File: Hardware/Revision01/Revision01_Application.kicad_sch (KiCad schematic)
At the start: 59 parts, among them J2 StrainConn, J3 StrainConn, J4 StrainConn, J5 StrainConn, J6 StrainConn, J7 StrainConn, J8 StrainConn, J9 StrainConn, Q3 NMOS, Q4 PMOS, Q6 PMOS, U11 LP5813BDRRR, U2 MRF89XAM9AT-I/RM, U4 ICM-45605, U6 INA317xxDGK

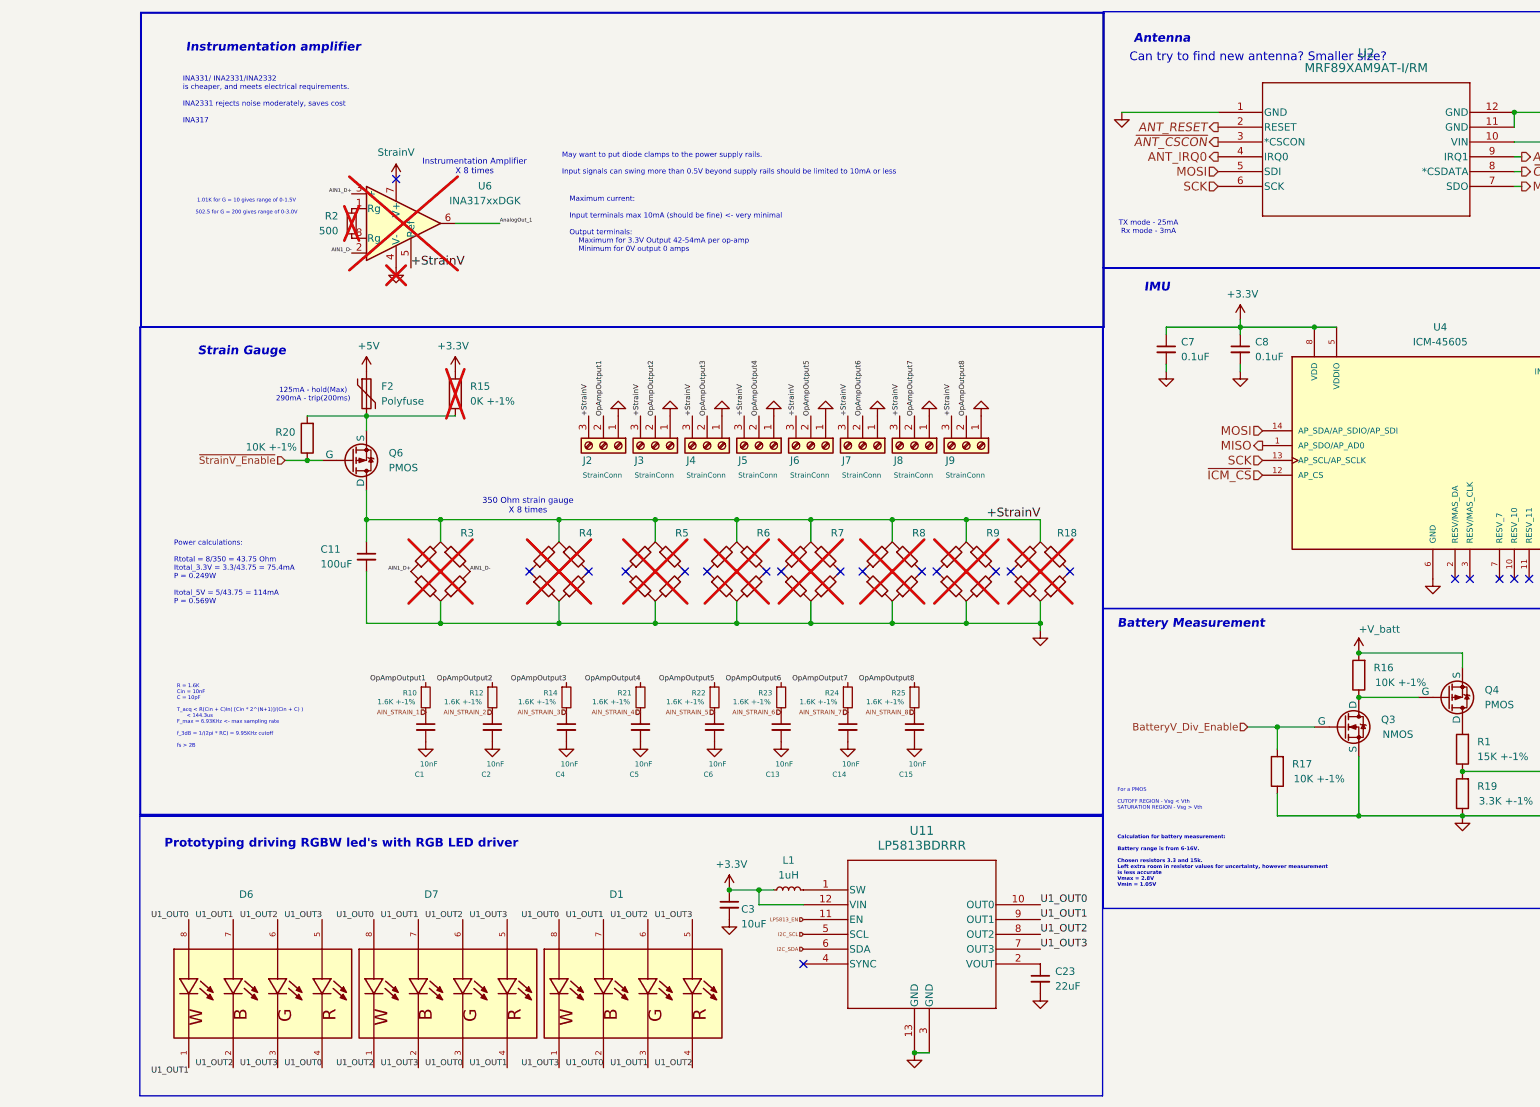
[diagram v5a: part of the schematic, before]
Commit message: schematic wiring, and LT-SPICE simulations on strain gauge - Added buffer with offset at 1.66V to instrumentation amplifier to ensure -20-20mv range can be read - Added caps to Instrumentation Amplifier circuit - Stimulated straingauge->Amplifier->Adc with all components imported. Verified ADC can read between 0.3-3.0V - Created second draft bom, component cost at around 212$ - Changed many components to Automotive grade - Added breathingCUBE led driver to prototype my own project
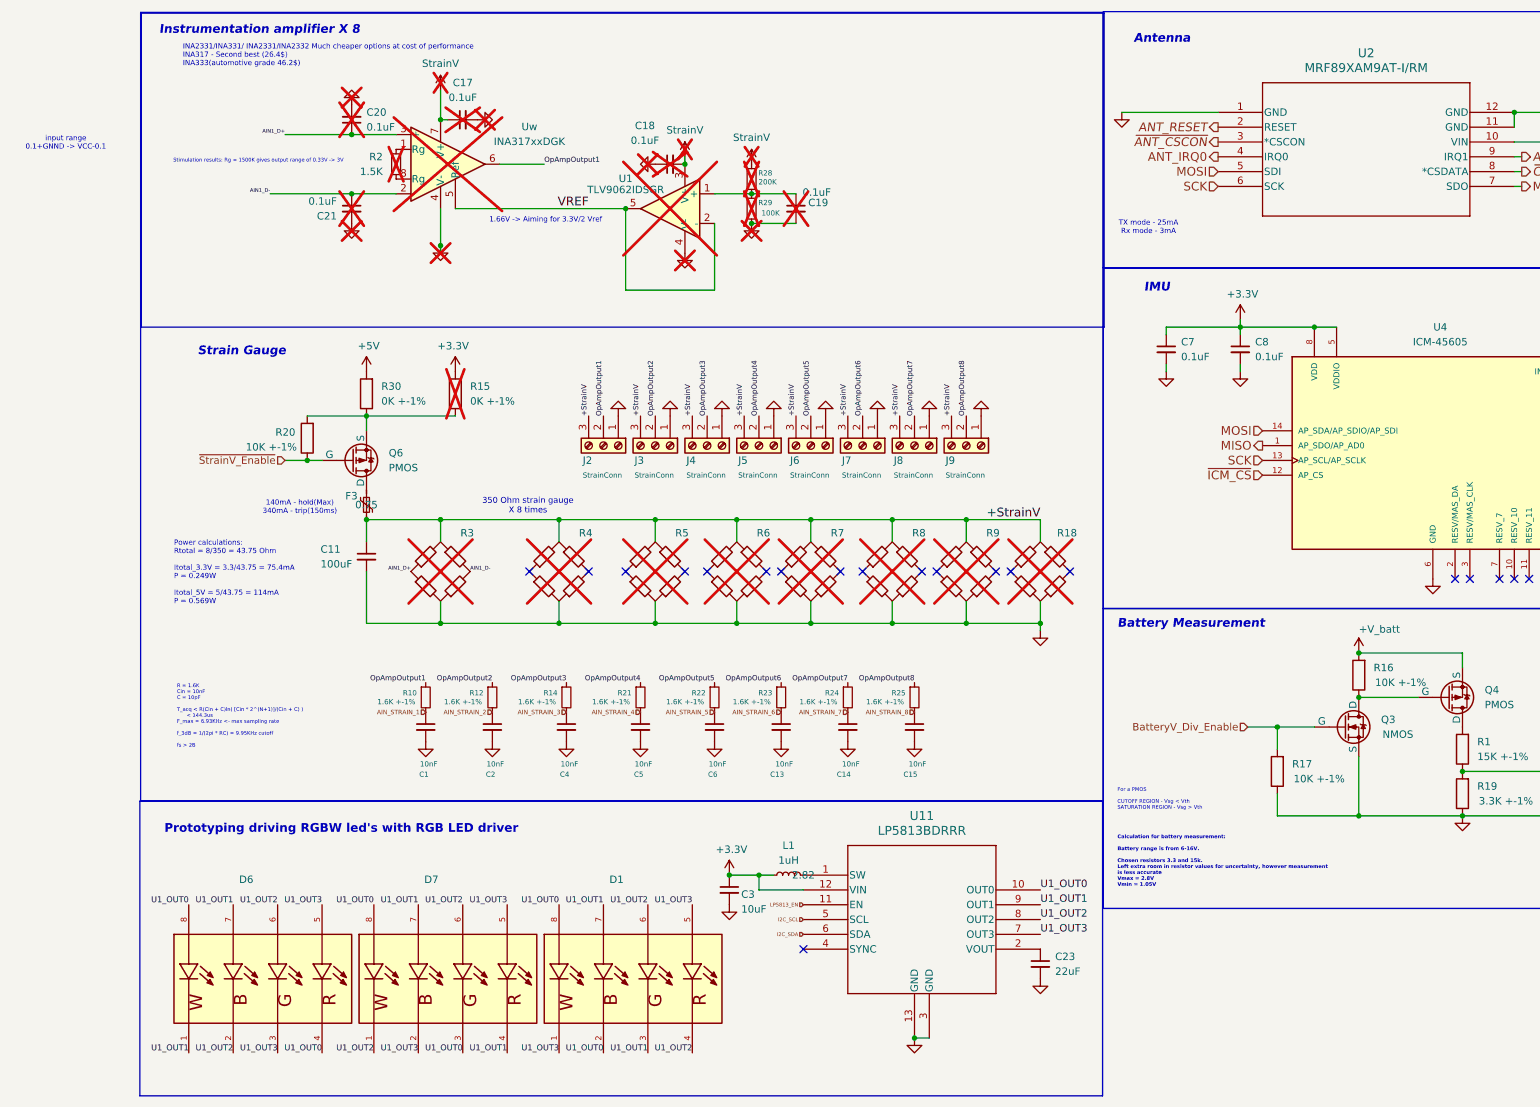
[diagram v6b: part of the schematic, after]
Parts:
- removed F2: Polyfuse, Resistor_SMD:R_1206_3216Metric_Pad1.30x1.75mm_HandSolder, symbol Device:Polyfuse
- added C17, C18, C19, C20, C21: 0.1uF, Capacitor_SMD:C_0805_2012Metric_Pad1.18x1.45mm_HandSolder, symbol Device:C_Small
- added F3: Polyfuse_Small, Resistor_SMD:R_1812_4532Metric_Pad1.30x3.40mm_HandSolder, symbol Device:Polyfuse_Small
- added R28: 200K, Resistor_SMD:R_0603_1608Metric_Pad0.98x0.95mm_HandSolder, symbol Device:R_Small
- added R29: 100K, Resistor_SMD:R_0603_1608Metric_Pad0.98x0.95mm_HandSolder, symbol Device:R_Small
- added R30: 0K +-1%, Resistor_SMD:R_1206_3216Metric_Pad1.30x1.75mm_HandSolder, symbol Device:R
- added U1: TLV9062IDSGR, symbol Simulation_SPICE:OPAMP
- C1, C13, C14, C15, C2, C4, C5, C6: Price per unit (none) -> 0.24700
- C10: Price per unit 0.15 -> 4; Quantity 3 -> (none)
- C11, Q3, R19, U2, U4: Quantity 1 -> (none)
- C12, C7, C8, C9: Distributor link https://www.digikey.ca/en/products/detail/yageo/CC0805JRNPO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 -> https://www.digikey.ca/en/products/detail/murata-electronic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; Manufacturer Samsung Electro-Mechanics -> Murata Electronics; Manufacturer Part Number CL05B104KA5NNNC -> GCM155R71C104KA55J; Price per unit 0.12 -> 0.043; Quantity 23 -> (none)
- C23: Price per unit (none) -> 0.12000
- C3: Distributor link (none) -> https://www.digikey.ca/en/products/detail/murata-electronic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; Manufacturer Part Number (none) -> CL31B106KAHNNNE; Price per unit (none) -> 4
- D1, D6, D7: Distributor link (none) -> https://www.digikey.ca/en/products/detail/qt-brightek-qtb/Q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; Price per unit (none) -> 1.19000
- L1: Price per unit (none) -> 0.36000
- Q4, Q6: Quantity 2 -> (none)
- R1: footprint Resistor_SMD:R_0805_2012Metric -> Resistor_SMD:R_0603_1608Metric_Pad0.98x0.95mm_HandSolder; Quantity 1 -> (none)
- R10, R12, R14, R21, R22, R23, R24, R25: footprint Resistor_SMD:R_0815_2038Metric -> Resistor_SMD:R_0402_1005Metric_Pad0.72x0.64mm_HandSolder; Distributor link https://www.digikey.ca/en/products/detail/yageo/RC0805FR-07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 -> https://www.digikey.ca/en/products/detail/yageo/RC0402FR-07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; Manufacturer Part Number RC0805FR-071K6L -> RC0402FR-071K6L; Price per unit (none) -> 0.012
- R15: Price per unit 0.42 -> 0.27; Quantity 2 -> (none)
- R16, R17: footprint Resistor_SMD:R_2512_6332Metric_Pad1.40x3.35mm_HandSolder -> Resistor_SMD:R_0603_1608Metric_Pad0.98x0.95mm_HandSolder; Distributor link https://www.digikey.ca/en/products/detail/yageo/RC0805FR-07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 -> https://www.digikey.ca/en/products/detail/bourns-inc/CR0603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; Manufacturer (none) -> Bourns Inc; Manufacturer Part Number CRGCQ2512F10K -> CR0603-FX-1002ELF; Quantity 3 -> (none)
- R2: value 500 -> 1.5K; Distributor link (none) -> https://www.mouser.ca/ProductDetail/KOA-Speer/RN73H1JTTD150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; Manufacturer (none) -> KOA Speer; Manufacturer Part Number (none) -> RT0603BRC07500RL; Price per unit (none) -> 0.098
- R20: footprint Resistor_SMD:R_2512_6332Metric_Pad1.40x3.35mm_HandSolder -> Resistor_SMD:R_0603_1608Metric_Pad0.98x0.95mm_HandSolder; Distributor link https://www.digikey.ca/en/products/detail/te-connectivity-p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 -> https://www.digikey.ca/en/products/detail/bourns-inc/CR0603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; Manufacturer (none) -> Bourns Inc; Manufacturer Part Number CRGCQ2512F10K -> CR0603-FX-1002ELF; Quantity 3 -> (none)
- U11: Distributor link (none) -> https://www.mouser.ca/ProductDetail/Texas-Instruments/LP581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; Price per unit (none) -> 2.82
- Uw: renamed from U6; Distributor link (none) -> https://www.mouser.ca/ProductDetail/Texas-Instruments/INA31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; Manufacturer (none) -> Texas Instruments; Manufacturer Part Number (none) -> INA317IDGKR; Price per unit (none) -> 2.64
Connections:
- net AnalogOut_1 is gone; now on net OpAmpOutput1: Uw.6
- net +5V: now also R30.2
- net +StrainV: now also F3.2; no longer Q6.1 (D), Uw.5 (Ref)
- net AIN1_D+: now also C20.1
- net AIN1_D-: now also C21.1
- net GND: now also C17.2, C18.1, C19.2, C20.2, C21.2, R29.2, U1.4 (V-)
- net U1_OUT1: now also D6.1
- net at Q6.3 (S), R15.1, R20.2: now also R30.1
- net at Uw.7 (V+): now also C17.1
- new net: F3.1, Q6.1 (D)
- new net: C19.1, R28.2, R29.1, U1.1 (+)
- new net: C18.2, U1.3 (V+)
- new net VREF: U1.2 (-), U1.5, Uw.5 (Ref)
- no-connect marks 21 -> 20
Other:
- note added: "1.66V -> Aiming for 3.3V/2 Vref"
- note added: "140mA - hold(Max) 340mA - trip(150ms)"
- note added: "INA2331/INA331/ INA2331/INA2332 Much cheaper options at cost of performance INA317 - Second best (26.4$) INA333(automotive grade 46.2$)"
- note added: "Instrumentation amplifier X 8"
- note added: "Stimulation results: Rg = 1500K gives output range of 0.33V -> 3V"
- note added: "input range 0.1+GNND -> VCC-0.1"
- note removed: "1.01K for G = 10 gives range of 0-1.5V 502.5 for G = 200 gives range of 0-3.0V"
- note removed: "125mA - hold(Max) 290mA - trip(200ms)"
- note removed: "Can try to find new antenna? Smaller size?"
- note removed: "INA331/ INA2331/INA2332 is cheaper, and meets electrical requirements. INA2331 rejects noise moderately, saves cost INA317"
- note removed: "Instrumentation Amplifier X 8 times"
- note removed: "Instrumentation amplifier"
- note removed: "Maximum current: Input terminals max 10mA (should be fine) <- very minimal Output terminals: Maximum for 3.3V Output 42-54mA per op-amp Minimum for 0V output 0 amps"
- note removed: "May want to put diode clamps to the power supply rails. Input signals can swing more than 0.5V beyond supply rails should be limited to 10mA or less"
- moved on the sheet: C23, C3, D1, D6, D7, L1, R2, U11, Uw

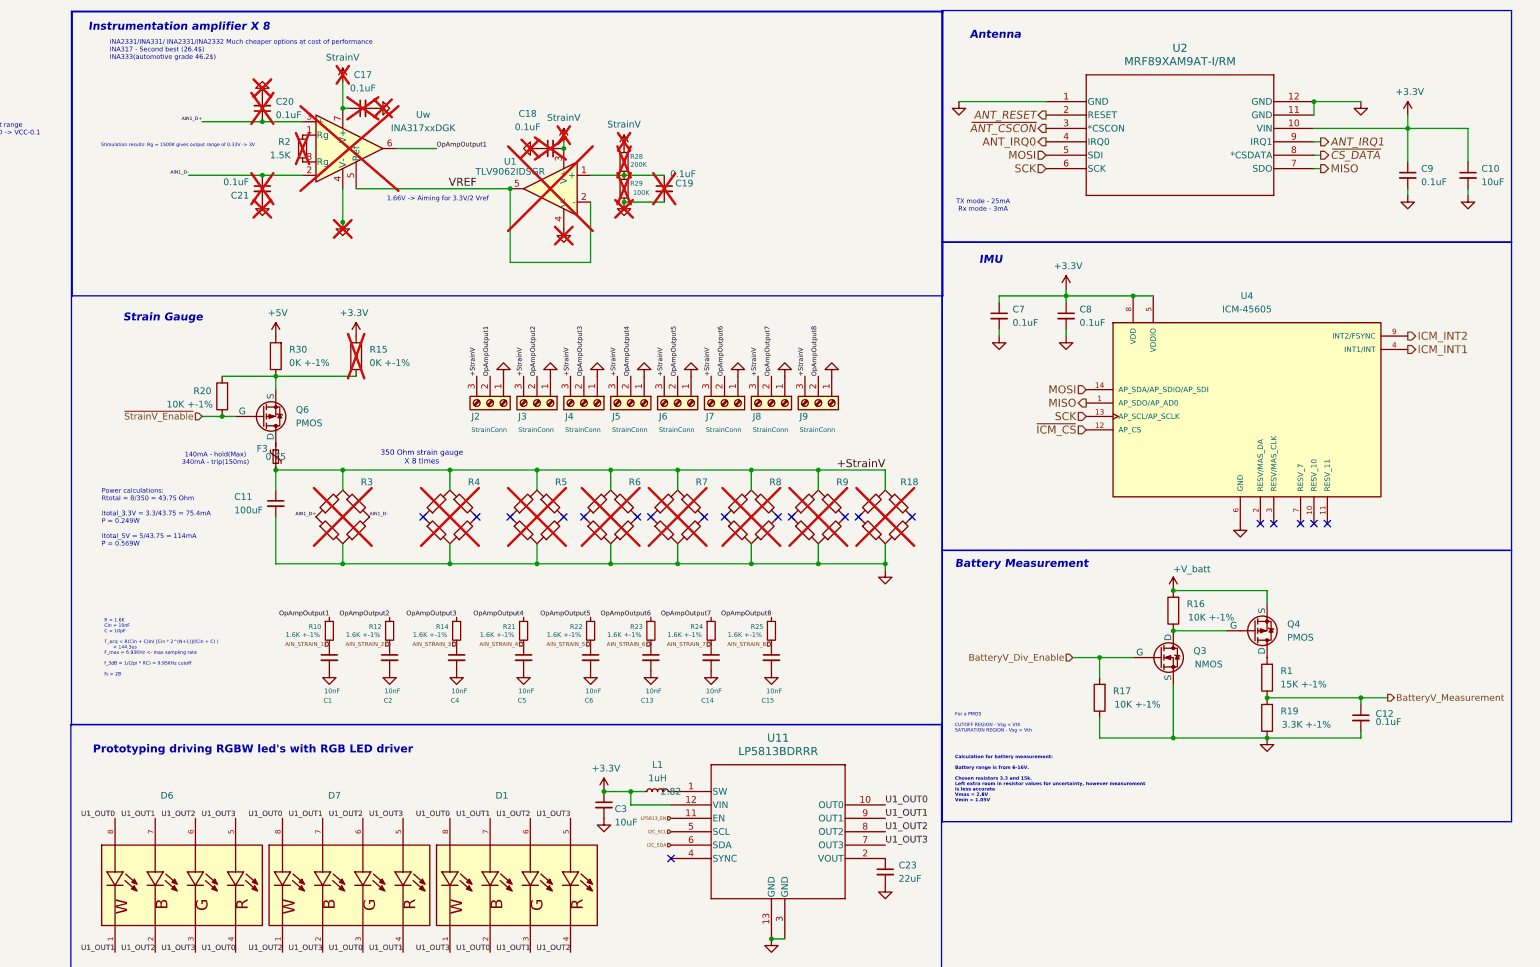
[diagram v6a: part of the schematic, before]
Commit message: branch fuses selected. Ready for PCB layout
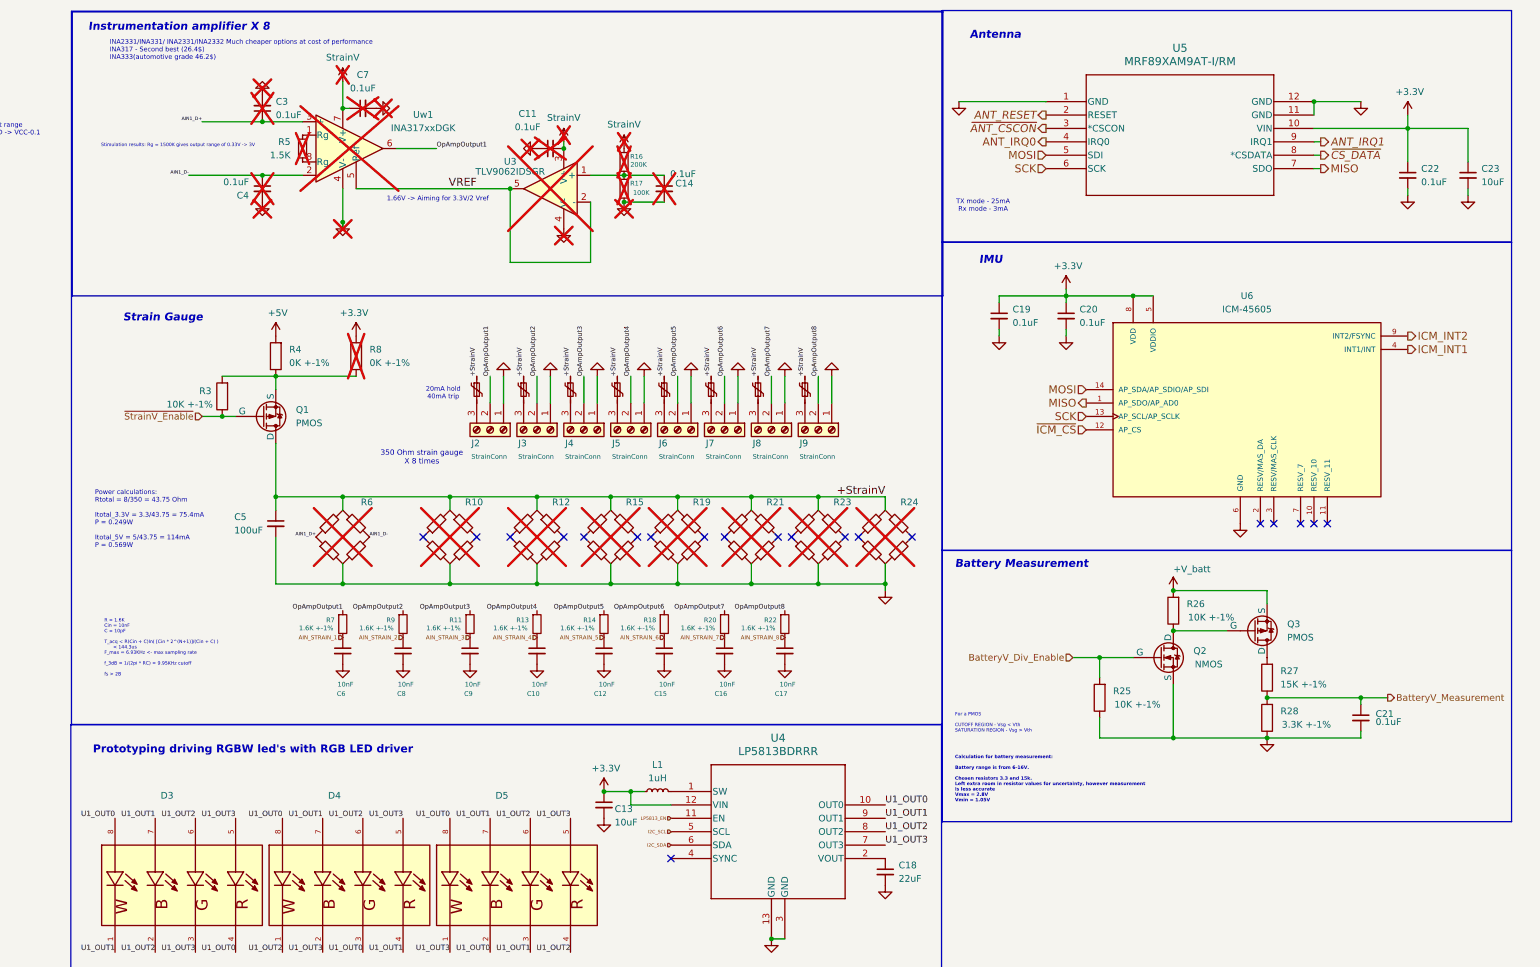
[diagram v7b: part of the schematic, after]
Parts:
- added F3, F4, F5, F6, F7, F8, F9: Polyfuse_Small, Resistor_SMD:R_0603_1608Metric_Pad0.98x0.95mm_HandSolder, symbol Device:Polyfuse_Small
- C13: renamed from C3; footprint Capacitor_SMD:C_0402_1005Metric_Pad0.74x0.62mm_HandSolder -> Capacitor_SMD:C_1206_3216Metric_Pad1.33x1.80mm_HandSolder; Distributor link https://www.digikey.ca/en/products/detail/murata-electronic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 -> https://www.digikey.ca/en/products/detail/samsung-electro-m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; Price per unit 4 -> 0.15
- C23: renamed from C10; footprint Capacitor_SMD:C_1206_3216Metric -> Capacitor_SMD:C_1206_3216Metric_Pad1.33x1.80mm_HandSolder; Distributor link https://www.digikey.ca/en/products/detail/murata-electronic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 -> https://www.digikey.ca/en/products/detail/samsung-electro-m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; Price per unit 4 -> 0.15
- F2: renamed from F3; footprint Resistor_SMD:R_1812_4532Metric_Pad1.30x3.40mm_HandSolder -> Resistor_SMD:R_0603_1608Metric_Pad0.98x0.95mm_HandSolder; Distributor link https://www.digikey.ca/en/products/detail/littelfuse-inc/18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 -> https://www.digikey.ca/en/products/detail/epcos-tdk-electro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; Manufacturer Part Number 1812L014DR -> B59622A0090A062
- U6: renamed from U4; footprint ICM-45605:XDCR_ICM-45605 -> ICM-45605-gyroscope:XDCR_ICM-45605
- renumbered C5 to C10, C18 to C11, C6 to C12, C19 to C14, C13 to C15, C14 to C16, C15 to C17, C23 to C18, C7 to C19, C8 to C20, C12 to C21, C9 to C22, C20 to C3, C21 to C4, C11 to C5, C1 to C6, C17 to C7, C2 to C8, C4 to C9, D6 to D3, D7 to D4, D1 to D5, Q6 to Q1, Q3 to Q2, Q4 to Q3, R4 to R10, R14 to R11, R5 to R12, R21 to R13, R22 to R14, R6 to R15, R28 to R16, R29 to R17, R23 to R18, R7 to R19, R24 to R20, R8 to R21, R25 to R22, R9 to R23, R18 to R24, R17 to R25, R16 to R26, R1 to R27, R19 to R28, R20 to R3, R30 to R4, R2 to R5, R3 to R6, R10 to R7, R15 to R8, R12 to R9, U1 to U3, U11 to U4, U2 to U5, Uw to Uw1
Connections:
- net +StrainV: now also F2.1, Q1.1 (D), F3.1, F4.1, F5.1, F6.1, F7.1, F8.1, F9.1; no longer F2.2, J2.3 (Pin_3), J3.3 (Pin_3), J4.3 (Pin_3), J5.3 (Pin_3), J6.3 (Pin_3), J7.3 (Pin_3), J8.3 (Pin_3), J9.3 (Pin_3)
- new net: F2.2, J2.3 (Pin_3)
- new net: F9.2, J9.3 (Pin_3)
- new net: F6.2, J6.3 (Pin_3)
- new net: F4.2, J4.3 (Pin_3)
- new net: F5.2, J5.3 (Pin_3)
- new net: F7.2, J7.3 (Pin_3)
- new net: F8.2, J8.3 (Pin_3)
- new net: F3.2, J3.3 (Pin_3)
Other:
- note added: "20mA hold 40mA trip"
- note removed: "140mA - hold(Max) 340mA - trip(150ms)"
- moved on the sheet: C10, C12, C15, C16, C17, C5, C6, C8, C9, J2, J3, J4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
